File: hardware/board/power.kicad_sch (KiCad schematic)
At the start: 11 parts, among them J1 Power, U3 TL074

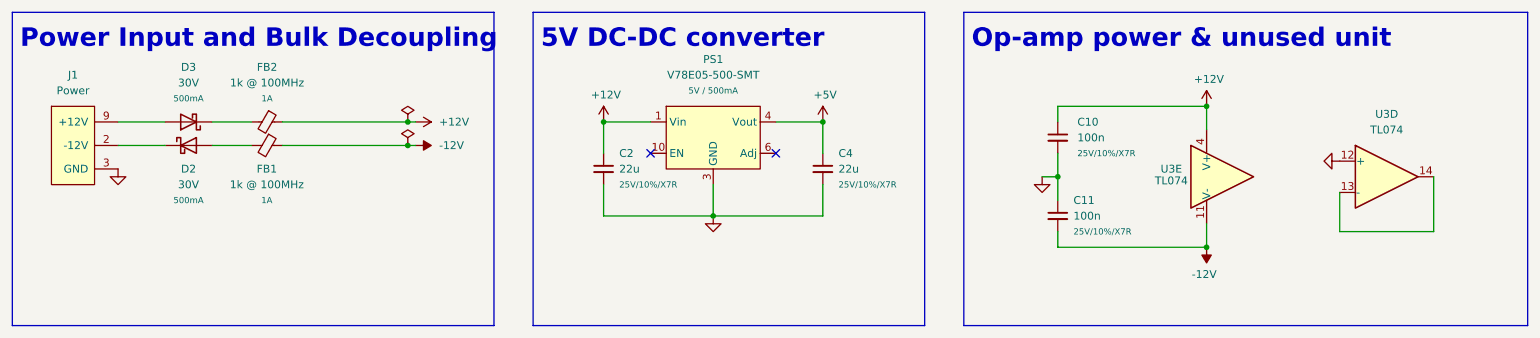
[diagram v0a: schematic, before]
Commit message: Hardware v10:
- Replaced EOL 5V DC-DC converter with new TI part.
- Re-drawn schematic to current Winterbloom standards and style.
- Improved layout and color-coding.
- Updated branding and silk screen.
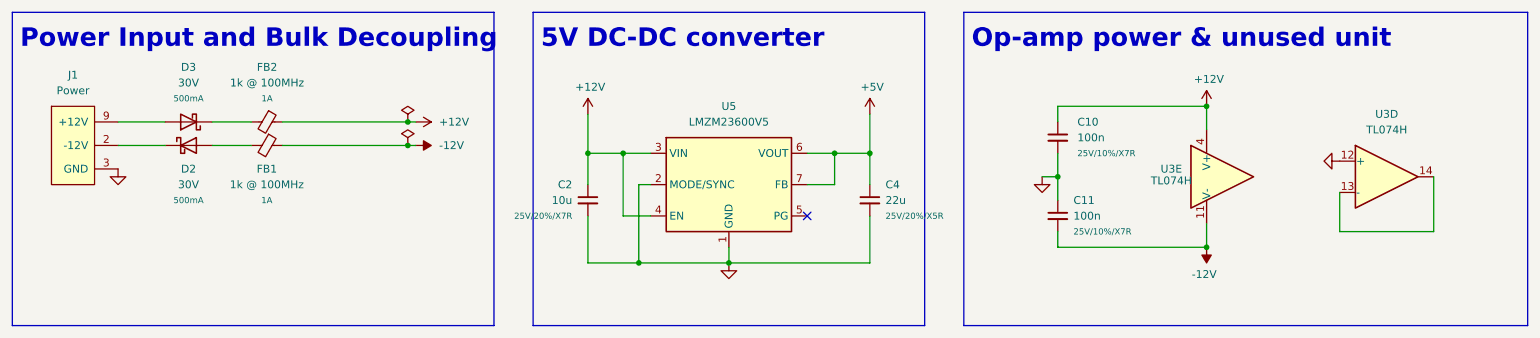
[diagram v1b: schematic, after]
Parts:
- removed PS1: V78E05-500-SMT, winterbloom:Converter_DCDC_CUI_V78E05-500-SMT, symbol winterbloom:V78E05-500-SMT
- added U5: LMZM23600V5, Package_LGA:Texas_SIL0010A_MicroSiP-10-1EP_3.8x3mm_P0.6mm_EP0.7x2.9mm_ThermalVias, symbol Regulator_Switching:LMZM23600V5
- C10, C11: LCSC (none) -> C1591; MPN (none) -> CL10B104KB8NNNC; Notes Bulk cap -> Bypass cap
- C2: value 22u -> 10u; footprint winterbloom:C_0805_HandSolder -> winterbloom:C_1210_HandSolder; Rating 25V/10%/X7R -> 25V/20%/X7R; Substitutes Allowed Yes -> Ask
- C4: LCSC (none) -> C45783; MPN (none) -> CL21A226MAQNNNE; Rating 25V/10%/X7R -> 25V/20%/X5R
- FB1, FB2: DigiKey 490-5212-1-ND -> (none); LCSC C97851 -> C160982; MPN BLM18BD121SN1D -> BLM18KG102SN1D
- U3: value TL074 -> TL074H; Substitutes Allowed (none) -> No; mpn TL074CPW -> (none); populate 1 -> (none)
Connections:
- net +12V: now also U5.3 (VIN), U5.4 (EN)
- net +5V: now also U5.6 (VOUT), U5.7 (FB)
- net GND: now also U5.1 (GND), U5.11 (GND), U5.2 (MODE/SYNC)
- no-connect marks 2 -> 1
